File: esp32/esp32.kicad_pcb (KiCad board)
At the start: 2 copper layers, 37 x 17 mm, 24 parts, among them J1 Conn_01x06_Pin, J2 Conn_01x06_Pin, J4 Conn_01x06_Pin, J5 USB_C_Receptacle_USB2.0_14P, Q1 MMSS8050, Q2 MMSS8050, SW1 XUNPU TS-1088R-02526, U1 SPX3819M5-L-3-3, U2 CP2102N-Axx-xQFN28

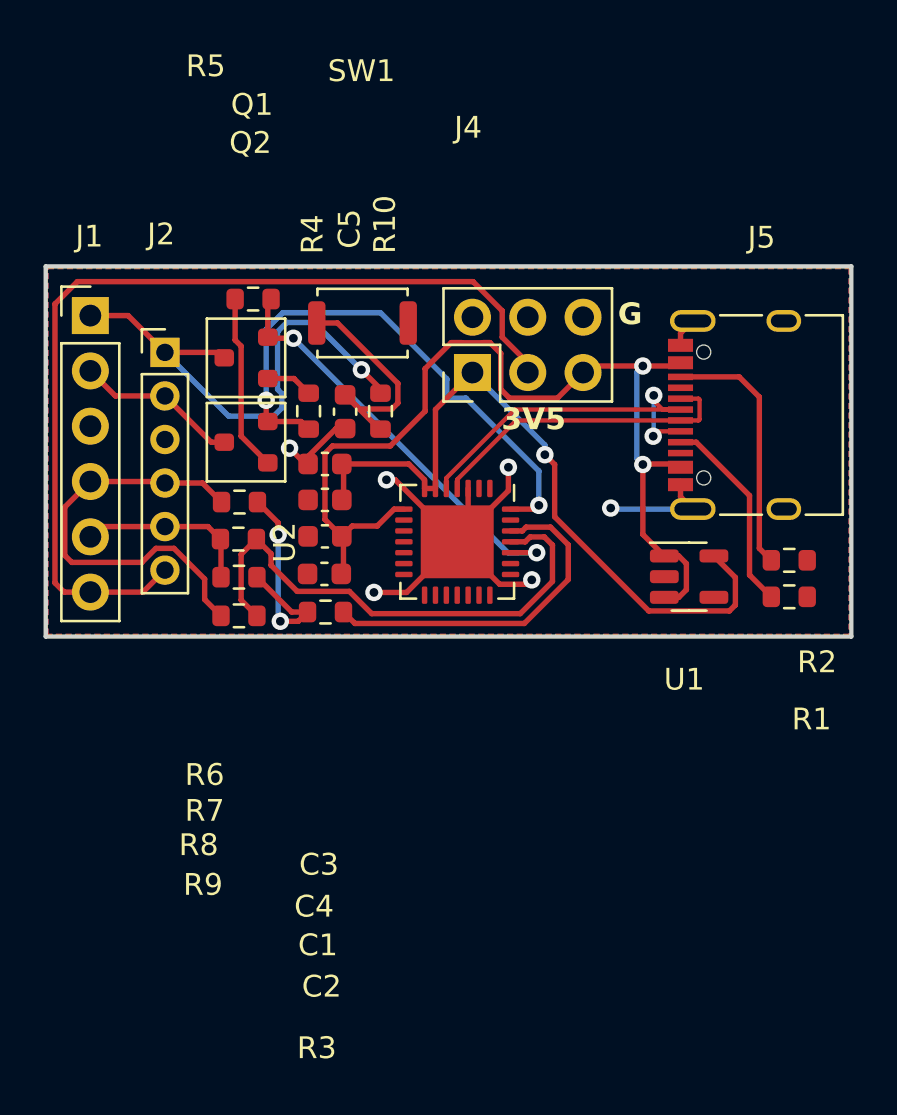
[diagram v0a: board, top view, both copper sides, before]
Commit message: esp32: reduce board length
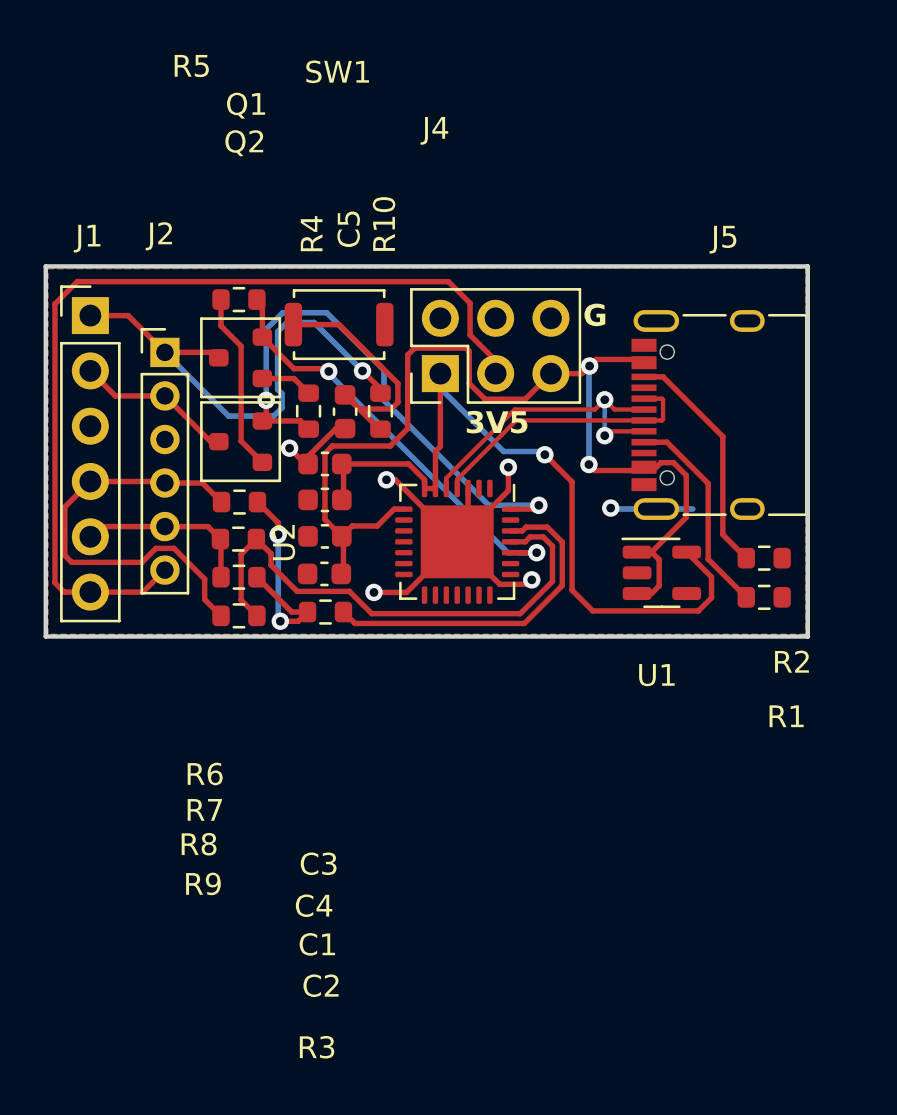
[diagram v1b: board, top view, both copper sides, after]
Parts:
- moved J5 1.67 mm to (131.2, 66.8)
- moved J4 1.48 mm to (118.1, 64.9)
- moved U1 1.26 mm to (128.3, 74.1)
- moved R1 1.15 mm to (133.0, 73.4)
- moved R2 1.15 mm to (133.0, 75.2)
- moved SW1 1.08 mm to (113.5, 62.7)
- moved R5 0.65 mm to (108.9, 61.5)
- moved Q2 0.25 mm to (109.0, 68.0)
- moved Q1 0.25 mm to (109.0, 64.2)
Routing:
- net GND: track 31.1 -> 28.1 mm
- net /D-: track 17.4 -> 14.8 mm
- net /D+: track 14.5 -> 12.8 mm
- net /5V: track 46.1 -> 47.8 mm
- net /3V3: track 33.8 -> 35.2 mm
- net /VOUT: track 43.3 -> 42.1 mm
- net Net-(C5-Pad2): track 10.9 -> 11.9 mm
- net Net-(J5-CC2): track 11.7 -> 10.8 mm
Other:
- board size 37 x 17 mm -> 35 x 17 mm

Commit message: esp32: move trace away from board edge
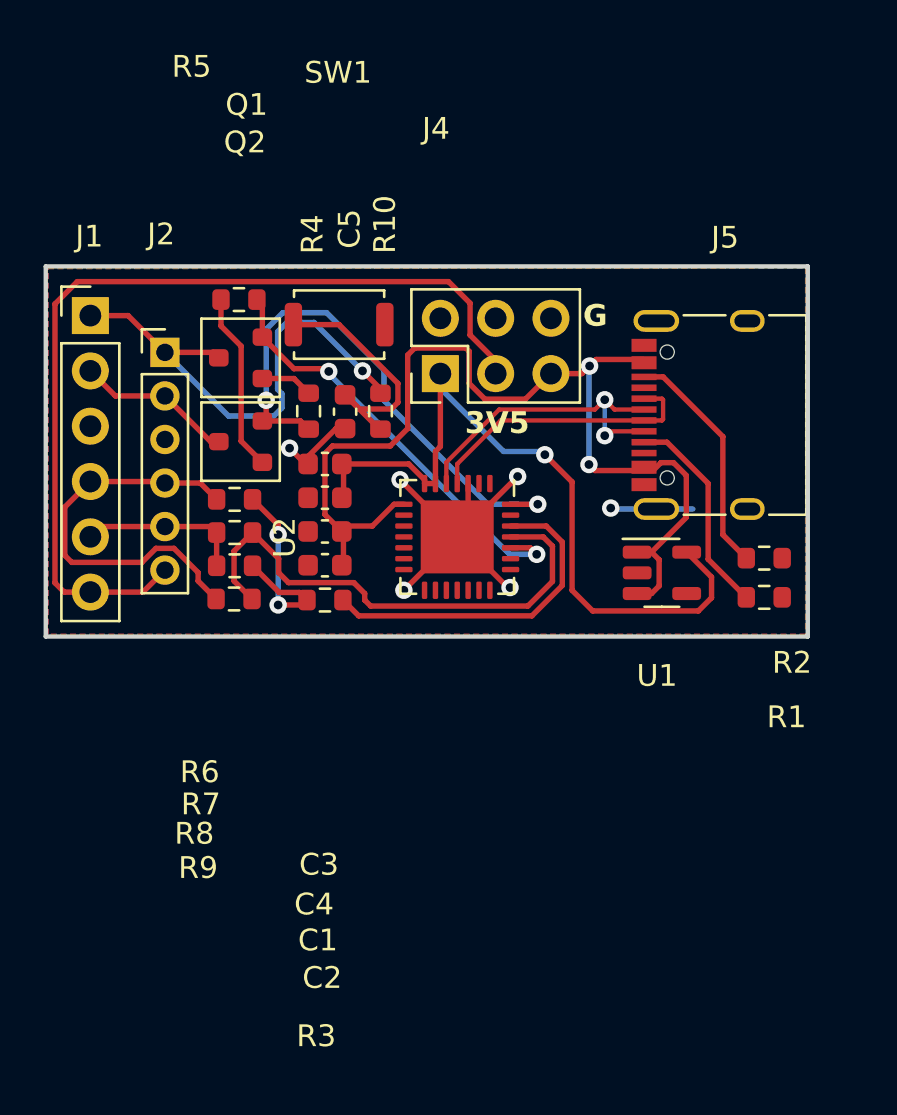
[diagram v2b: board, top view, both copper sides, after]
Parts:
- moved R9 0.81 mm to (108.7, 75.3)
- moved R8 0.56 mm to (108.7, 73.8)
- moved R3 0.55 mm to (112.8, 75.3)
- moved C2 0.40 mm to (112.8, 73.7)
- moved R7 0.35 mm to (108.7, 72.2)
- moved R6 0.26 mm to (108.7, 70.7)
- moved C1 0.23 mm to (112.8, 72.2)
- moved U2 0.23 mm to (118.9, 72.4)
- moved C4 0.10 mm to (112.8, 70.6)
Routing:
- net GND: track 28.1 -> 24.7 mm
- net /RX: track 19.7 -> 18.6 mm
- net /3V3: track 35.2 -> 34.6 mm
- net /TX: track 8.17 -> 7.63 mm

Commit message: esp32: move trace away from board edge
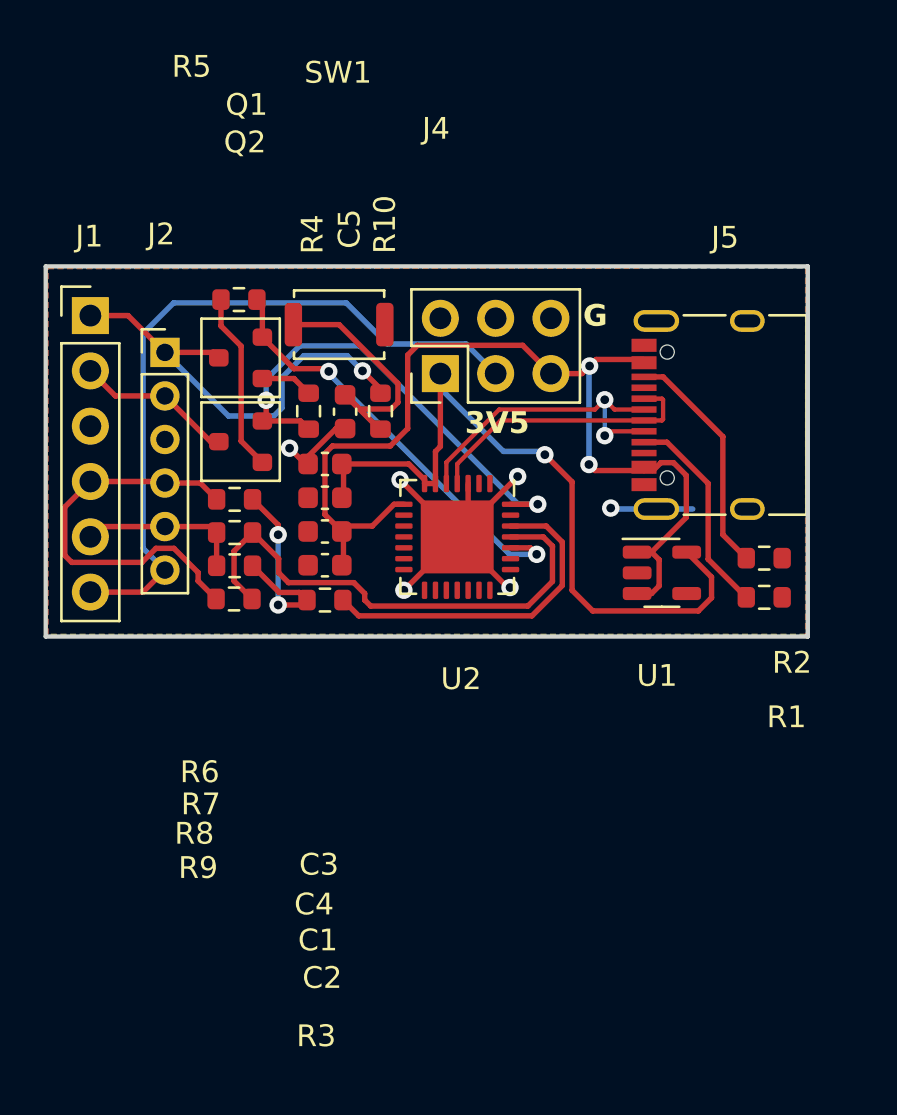
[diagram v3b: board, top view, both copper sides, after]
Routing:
- net /VOUT: track 42.1 -> 33.2 mm
- net /DTR: track 25.1 -> 21.6 mm
- net /EN: track 23.4 -> 20.6 mm
- net /5V: track 47.4 -> 45.6 mm

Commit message: update with kicad 8
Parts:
- Q1, Q2: footprint Package_TO_SOT_SMD_AKL:SOT-23 -> Package_TO_SOT_SMD:SOT-23
- moved J4 0.38 mm to (118.5, 64.9)
- moved SW1 0.28 mm to (113.8, 62.7)
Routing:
- net Net-(Q2-B): track 8.26 -> 15.1 mm, vias 0 -> 2
- net /VOUT: track 33.2 -> 34.8 mm
- net /5V: track 45.6 -> 46.4 mm
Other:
- board text added: "3 V 5"
- board text removed: "3V5"

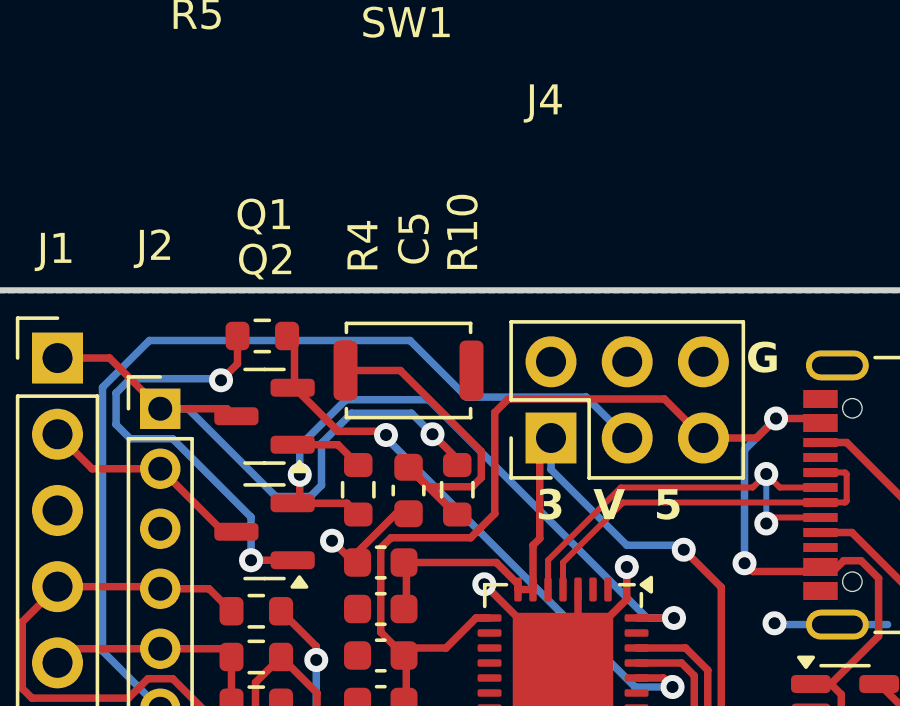
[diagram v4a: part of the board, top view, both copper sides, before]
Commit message: esp32: fix reset button
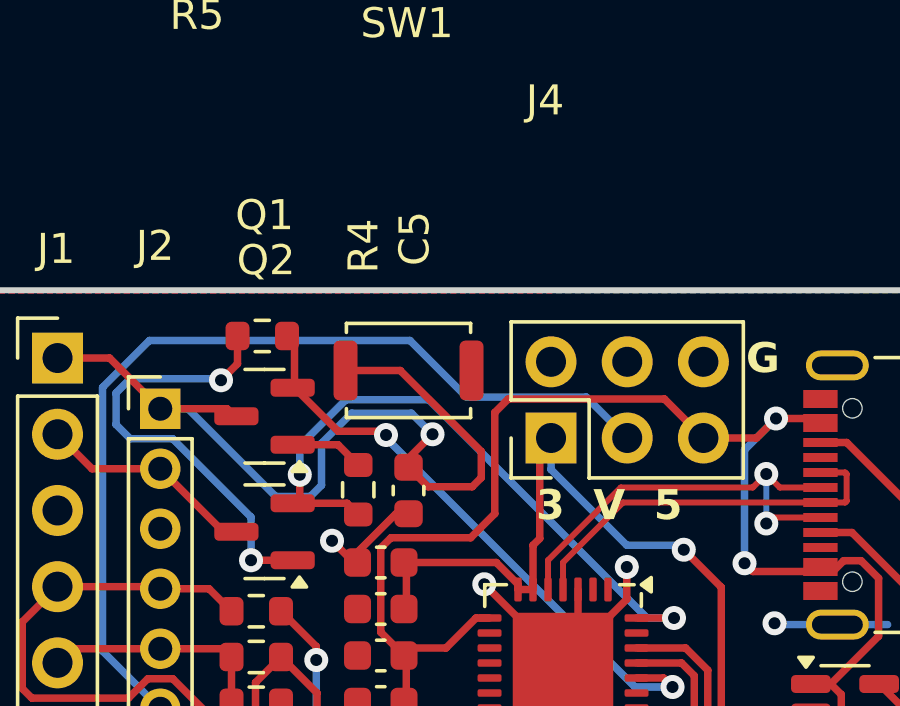
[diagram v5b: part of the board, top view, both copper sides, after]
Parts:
- removed R10: 470, Resistor_SMD:R_0603_1608Metric
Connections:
- C5 pad 2: Net-(C5-Pad2) -> /EN
- SW1 pad 2: Net-(C5-Pad2) -> /EN
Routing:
- net Net-(C5-Pad2): track 11.6 -> 0.00 mm
- net /EN: track 20.6 -> 30.0 mm
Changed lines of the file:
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@@
 	(net 37 "unconnected-(U2-~{CTS}-Pad23)")
 	(net 38 "unconnected-(U2-~{DSR}-Pad27)")
-	(net 39 "Net-(C5-Pad2)")
 	(footprint "Resistor_SMD:R_0603_1608Metric"
 		(layer "F.Cu")
@@
 		(sheetname "Root")
 		(sheetfile "esp32.kicad_sch")
-		(attr through_hole dnp)
+		(attr through_hole)
 		(fp_line
 			(start -1.06 -1.06)
@@
 		(sheetname "Root")
 		(sheetfile "esp32.kicad_sch")
-		(attr through_hole dnp)
+		(attr through_hole)
 		(fp_line
 			(start -1.33 -1.33)
@@
 			(layers "F.Cu" "F.Paste" "F.Mask")
 			(roundrect_rratio 0.25)
-			(net 39 "Net-(C5-Pad2)")
+			(net 4 "/EN")
 			(pinfunction "2")
 			(pintype "passive")
@@
 		)
 	)
-	(footprint "Resistor_SMD:R_0603_1608Metric"
-		(layer "F.Cu")
-		(at 115.375 66.65 90)
-		(descr "Resistor SMD 0603 (1608 Metric), square (rectangular) end terminal, IPC_7351 nominal, (Body size source: IPC-SM-782 page 72, https://www.pcb-3d.com/wordpress/wp-content/uploads/ipc-sm-782a_amendment_1_and_2.pdf), generated with kicad-footprint-generator")
-		(tags "resistor")
-		(property "Reference" "R10"
-			(at 8.575 0.2 90)
-			(layer "F.SilkS")
-			(effects
-				(font
-					(size 1 1)
-					(thickness 0.15)
-				)
-			)
-		)
-		(property "Value" "470"
-			(at 11.75 0.225 90)
-			(layer "F.Fab")
-			(effects
-				(font
-					(size 1 1)
-					(thickness 0.15)
-				)
-			)
-		)
-		(property "Footprint" "Resistor_SMD:R_0603_1608Metric"
-			(at 0 0 90)
-			(layer "F.Fab")
-			(hide yes)
-			(effects
-				(font
-					(size 1.27 1.27)
-					(thickness 0.15)
-				)
-			)
-		)
-		(property "Datasheet" ""
-			(at 0 0 90)
-			(layer "F.Fab")
-			(hide yes)
-			(effects
-				(font
-					(size 1.27 1.27)
-					(thickness 0.15)
-				)
-			)
-		)
-		(property "Description" ""
-			(at 0 0 90)
-			(layer "F.Fab")
-			(hide yes)
-			(effects
-				(font
-					(size 1.27 1.27)
-					(thickness 0.15)
-				)
-			)
-		)
-		(property ki_fp_filters "R_*")
-		(sheetname "Root")
-		(sheetfile "esp32.kicad_sch")
-		(attr smd)
-		(fp_line
-			(start -0.237258 -0.5225)
-			(end 0.237258 -0.5225)
-			(stroke
-				(width 0.12)
-				(type solid)
-			)
-			(layer "F.SilkS")
-		)
-		(fp_line
-			(start -0.237258 0.5225)
-			(end 0.237258 0.5225)
-			(stroke
-				(width 0.12)
-				(type solid)
-			)
-			(layer "F.SilkS")
-		)
-		(fp_line
-			(start 1.48 -0.73)
-			(end 1.48 0.73)
-			(stroke
-				(width 0.05)
-				(type solid)
-			)
-			(layer "F.CrtYd")
-		)
-		(fp_line
-			(start -1.48 -0.73)
-			(end 1.48 -0.73)
-			(stroke
-				(width 0.05)
-				(type solid)
-			)
-			(layer "F.CrtYd")
-		)
-		(fp_line
-			(start 1.48 0.73)
-			(end -1.48 0.73)
-			(stroke
-				(width 0.05)
-				(type solid)
-			)
-			(layer "F.CrtYd")
-		)
-		(fp_line
-			(start -1.48 0.73)
-			(end -1.48 -0.73)
-			(stroke
-				(width 0.05)
-				(type solid)
-			)
-			(layer "F.CrtYd")
-		)
-		(fp_line
-			(start 0.8 -0.4125)
-			(end 0.8 0.4125)
-			(stroke
-				(width 0.1)
-				(type solid)
-			)
-			(layer "F.Fab")
-		)
-		(fp_line
-			(start -0.8 -0.4125)
-			(end 0.8 -0.4125)
-			(stroke
-				(width 0.1)
-				(type solid)
-			)
-			(layer "F.Fab")
-		)
-		(fp_line
-			(start 0.8 0.4125)
-			(end -0.8 0.4125)
-			(stroke
-				(width 0.1)
-				(type solid)
-			)
-			(layer "F.Fab")
-		)
-		(fp_line
-			(start -0.8 0.4125)
-			(end -0.8 -0.4125)
-			(stroke
-				(width 0.1)
-				(type solid)
-			)
-			(layer "F.Fab")
-		)
-		(fp_text user "${REFERENCE}"
-			(at 0 0 90)
-			(layer "F.Fab")
-			(effects
-				(font
-					(size 0.4 0.4)
-					(thickness 0.06)
-				)
-			)
-		)
-		(pad "1" smd roundrect
-			(at -0.825 0 90)
-			(size 0.8 0.95)
-			(layers "F.Cu" "F.Paste" "F.Mask")
-			(roundrect_rratio 0.25)
-			(net 39 "Net-(C5-Pad2)")
-			(pintype "passive")
-		)
-		(pad "2" smd roundrect
-			(at 0.825 0 90)
-			(size 0.8 0.95)
-			(layers "F.Cu" "F.Paste" "F.Mask")
-			(roundrect_rratio 0.25)
-			(net 4 "/EN")
-			(pintype "passive")
-		)
-		(model "${KICAD8_3DMODEL_DIR}/Resistor_SMD.3dshapes/R_0603_1608Metric.wrl"
-			(offset
-				(xyz 0 0 0)
-			)
-			(scale
-				(xyz 1 1 1)
-			)
-			(rotate
-				(xyz 0 0 0)
-			)
-		)
-	)
 	(footprint "Capacitor_SMD:C_0603_1608Metric"
 		(layer "F.Cu")
@@
 			(layers "F.Cu" "F.Paste" "F.Mask")
 			(roundrect_rratio 0.25)
-			(net 39 "Net-(C5-Pad2)")
+			(net 4 "/EN")
 			(pintype "passive")
 		)
@@
 	)
 	(segment
+		(start 115.873004 66.55)
+		(end 116.175 66.248004)
+		(width 0.25)
+		(layer "F.Cu")
+		(net 4)
+	)
+	(segment
 		(start 103.785 62.26)
 		(end 105.475 63.95)
@@
 	)
 	(segment
+		(start 114.4 66.55)
+		(end 115.873004 66.55)
+		(width 0.25)
+		(layer "F.Cu")
+		(net 4)
+	)
+	(segment
 		(start 105.475 63.95)
 		(end 107.7 63.95)
@@
 	)
 	(segment
+		(start 113.75 65.9)
+		(end 114.4 66.55)
+		(width 0.25)
+		(layer "F.Cu")
+		(net 4)
+	)
+	(segment
 		(start 107.7 63.95)
 		(end 107.95 64.2)
@@
 	)
 	(segment
-		(start 115.375 65.625001)
-		(end 115.375 65.825)
+		(start 113.75 65.9)
+		(end 113.75 65.599999)
+		(width 0.25)
+		(layer "F.Cu")
+		(net 4)
+	)
+	(segment
+		(start 113.475 62.675)
+		(end 111.65 62.675)
 		(width 0.25)
 		(layer "F.Cu")
@@
 	)
 	(segment
-		(start 114.549999 64.8)
-		(end 115.375 65.625001)
+		(start 116.175 65.375)
+		(end 113.475 62.675)
+		(width 0.25)
+		(layer "F.Cu")
+		(net 4)
+	)
+	(segment
+		(start 116.175 66.248004)
+		(end 116.175 65.375)
+		(width 0.25)
+		(layer "F.Cu")
+		(net 4)
+	)
+	(segment
+		(start 113.75 65.599999)
+		(end 114.549999 64.8)
 		(width 0.25)
 		(layer "F.Cu")
@@
 		(net 19)
 	)
-	(segment
-		(start 115.873004 66.55)
-		(end 116.175 66.248004)
-		(width 0.25)
-		(layer "F.Cu")
-		(net 39)
-	)
-	(segment
-		(start 114.4 66.55)
-		(end 115.873004 66.55)
-		(width 0.25)
-		(layer "F.Cu")
-		(net 39)
-	)
-	(segment
-		(start 113.75 65.9)
-		(end 114.4 66.55)
-		(width 0.25)
-		(layer "F.Cu")
-		(net 39)
-	)
-	(segment
-		(start 113.475 62.675)
-		(end 111.65 62.675)
-		(width 0.25)
-		(layer "F.Cu")
-		(net 39)
-	)
-	(segment
-		(start 115.325 67.475)
-		(end 113.75 65.9)
-		(width 0.25)
-		(layer "F.Cu")
-		(net 39)
-	)
-	(segment
-		(start 116.175 65.375)
-		(end 113.475 62.675)
-		(width 0.25)
-		(layer "F.Cu")
-		(net 39)
-	)
-	(segment
-		(start 115.375 67.475)
-		(end 115.325 67.475)
-		(width 0.25)
-		(layer "F.Cu")
-		(net 39)
-	)
-	(segment
-		(start 116.175 66.248004)
-		(end 116.175 65.375)
-		(width 0.25)
-		(layer "F.Cu")
-		(net 39)
-	)
 	(zone
